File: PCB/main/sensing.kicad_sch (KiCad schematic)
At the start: 0 parts

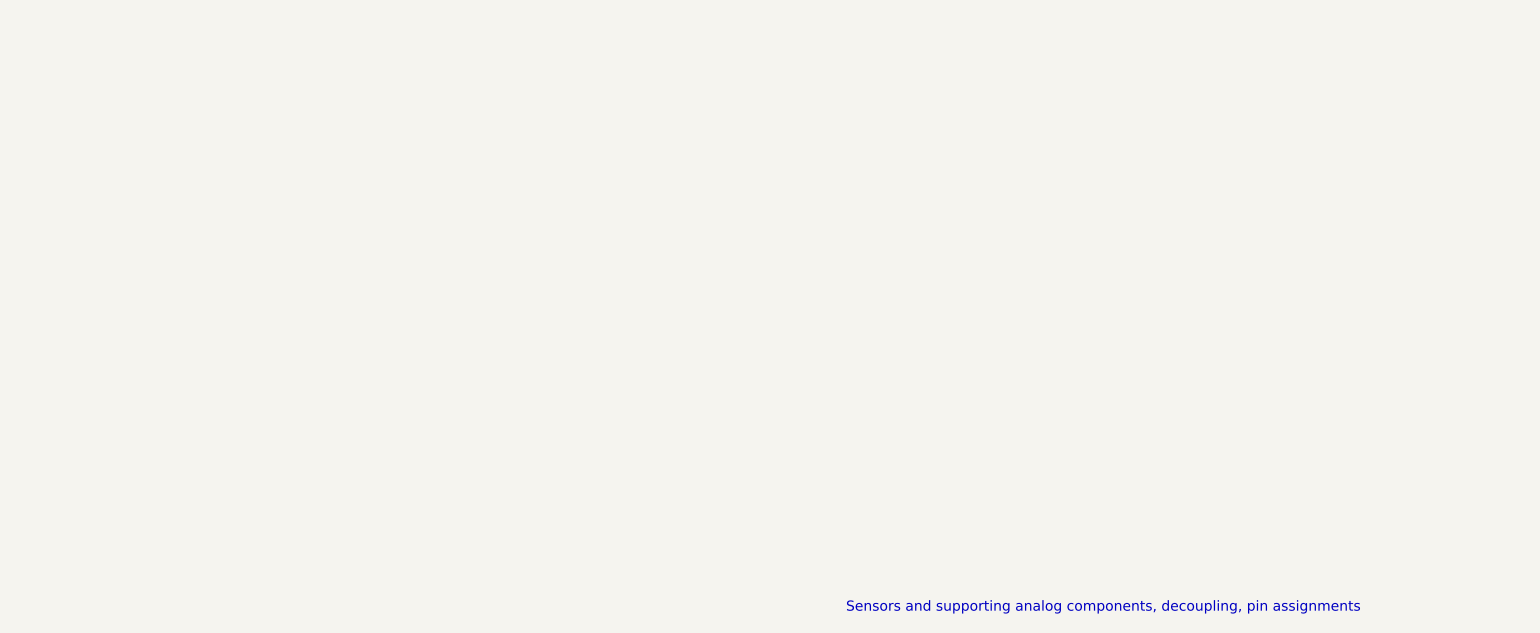
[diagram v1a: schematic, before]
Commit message: Added sensing schematic
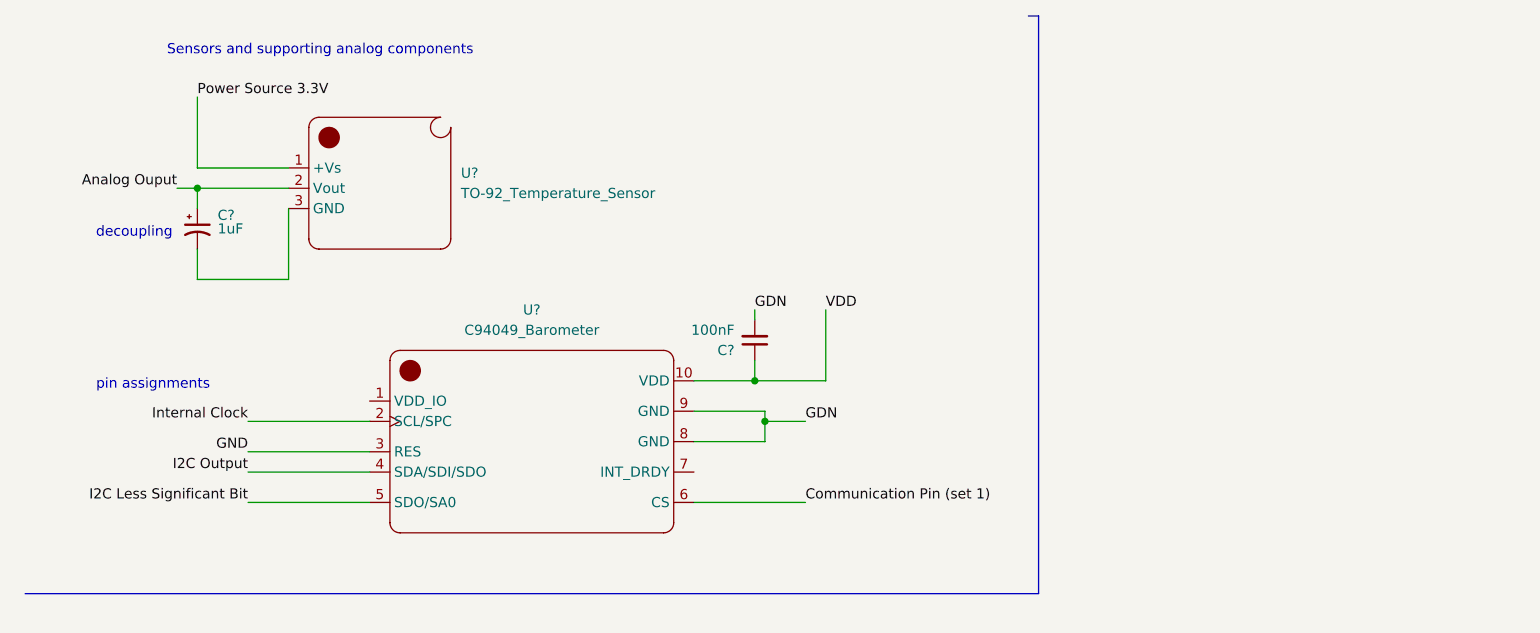
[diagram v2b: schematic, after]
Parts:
- added C?: 1uF, symbol Device:C_Polarized_Small_US
- added C?: 100nF, symbol Device:C_Small
- added U?: TO-92_Temperature_Sensor, symbol AAA 3088F:TO-92_Temperature_Sensor
- added U?: C94049_Barometer, symbol AAA 3088F:_C94049_Barometer
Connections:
- new net: C?.2, U?.3 (GND)
- new net Analog Ouput: C?.1, U?.2 (Vout)
- new net Communication Pin (set 1): U?.6 (CS)
- new net GDN: C?.2, U?.8 (GND), U?.9 (GND)
- new net GND: U?.3 (RES)
- new net I2C Less Significant Bit: U?.5 (SDO/SA0)
- new net I2C Output: U?.4 (SDA/SDI/SDO)
- new net Internal Clock: U?.2 (SCL/SPC)
- new net Power Source 3.3V: U?.1 (+Vs)
- new net VDD: C?.1, U?.10 (VDD)
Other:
- note added: "Sensors and supporting analog components"
- note added: "decoupling"
- note added: "pin assignments"
- note removed: "Sensors and supporting analog components, decoupling, pin assignments"
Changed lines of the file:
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@@
 (kicad_sch (version 20211123) (generator eeschema)
   (paper "A4")
-  (text "Sensors and supporting analog components, decoupling, pin assignments"
-    (at 115.57 86.36 0)
+  (junction (at 34.29 33.02) (diameter 0) (color 0 0 0 0)
+  )
+  (junction (at 105.41 62.23) (diameter 0) (color 0 0 0 0)
+  )
+  (junction (at 104.14 57.15) (diameter 0) (color 0 0 0 0)
+  )
+  (wire (pts (xy 104.14 57.15) (xy 104.14 54.61))
+    (stroke (width 0) (type default) (color 0 0 0 0))
+  )
+  (wire (pts (xy 96.52 57.15) (xy 104.14 57.15))
+    (stroke (width 0) (type default) (color 0 0 0 0))
+  )
+  (wire (pts (xy 31.75 33.02) (xy 34.29 33.02))
+    (stroke (width 0) (type default) (color 0 0 0 0))
+  )
+  (wire (pts (xy 40.64 68.58) (xy 55.88 68.58))
+    (stroke (width 0) (type default) (color 0 0 0 0))
+  )
+  (wire (pts (xy 105.41 64.77) (xy 105.41 62.23))
+    (stroke (width 0) (type default) (color 0 0 0 0))
+  )
+  (wire (pts (xy 40.64 62.23) (xy 55.88 62.23))
+    (stroke (width 0) (type default) (color 0 0 0 0))
+  )
+  (polyline (pts (xy 12.7 83.82) (xy 139.7 83.82))
+    (stroke (width 0) (type default) (color 0 0 0 0))
+  )
+  (wire (pts (xy 34.29 30.48) (xy 34.29 21.59))
+    (stroke (width 0) (type default) (color 0 0 0 0))
+  )
+  (wire (pts (xy 40.64 72.39) (xy 55.88 72.39))
+    (stroke (width 0) (type default) (color 0 0 0 0))
+  )
+  (wire (pts (xy 45.72 35.56) (xy 45.72 44.45))
+    (stroke (width 0) (type default) (color 0 0 0 0))
+  )
+  (wire (pts (xy 96.52 72.39) (xy 110.49 72.39))
+    (stroke (width 0) (type default) (color 0 0 0 0))
+  )
+  (wire (pts (xy 34.29 33.02) (xy 34.29 35.56))
+    (stroke (width 0) (type default) (color 0 0 0 0))
+  )
+  (wire (pts (xy 104.14 57.15) (xy 113.03 57.15))
+    (stroke (width 0) (type default) (color 0 0 0 0))
+  )
+  (wire (pts (xy 104.14 48.26) (xy 104.14 49.53))
+    (stroke (width 0) (type default) (color 0 0 0 0))
+  )
+  (wire (pts (xy 113.03 57.15) (xy 113.03 48.26))
+    (stroke (width 0) (type default) (color 0 0 0 0))
+  )
+  (polyline (pts (xy 139.7 83.82) (xy 139.7 11.43))
+    (stroke (width 0) (type default) (color 0 0 0 0))
+  )
+  (wire (pts (xy 96.52 60.96) (xy 105.41 60.96))
+    (stroke (width 0) (type default) (color 0 0 0 0))
+  )
+  (wire (pts (xy 105.41 62.23) (xy 110.49 62.23))
+    (stroke (width 0) (type default) (color 0 0 0 0))
+  )
+  (wire (pts (xy 105.41 60.96) (xy 105.41 62.23))
+    (stroke (width 0) (type default) (color 0 0 0 0))
+  )
+  (wire (pts (xy 45.72 30.48) (xy 34.29 30.48))
+    (stroke (width 0) (type default) (color 0 0 0 0))
+  )
+  (wire (pts (xy 40.64 66.04) (xy 55.88 66.04))
+    (stroke (width 0) (type default) (color 0 0 0 0))
+  )
+  (wire (pts (xy 45.72 44.45) (xy 34.29 44.45))
+    (stroke (width 0) (type default) (color 0 0 0 0))
+  )
+  (wire (pts (xy 34.29 40.64) (xy 34.29 44.45))
+    (stroke (width 0) (type default) (color 0 0 0 0))
+  )
+  (wire (pts (xy 96.52 64.77) (xy 105.41 64.77))
+    (stroke (width 0) (type default) (color 0 0 0 0))
+  )
+  (polyline (pts (xy 139.7 11.43) (xy 138.43 11.43))
+    (stroke (width 0) (type default) (color 0 0 0 0))
+  )
+  (wire (pts (xy 34.29 33.02) (xy 45.72 33.02))
+    (stroke (width 0) (type default) (color 0 0 0 0))
+  )
+  (text "Sensors and supporting analog components" (at 30.48 16.51 0)
     (effects (font (size 1.27 1.27)) (justify left bottom))
   )
+  (text "decoupling" (at 21.59 39.37 0)
+    (effects (font (size 1.27 1.27)) (justify left bottom))
+  )
+  (text "pin assignments" (at 21.59 58.42 0)
+    (effects (font (size 1.27 1.27)) (justify left bottom))
+  )
+  (label "Analog Ouput" (at 31.75 33.02 180)
+    (effects (font (size 1.27 1.27)) (justify right bottom))
+  )
+  (label "GND" (at 40.64 66.04 180)
+    (effects (font (size 1.27 1.27)) (justify right bottom))
+  )
+  (label "GDN" (at 104.14 48.26 0)
+    (effects (font (size 1.27 1.27)) (justify left bottom))
+  )
+  (label "Power Source 3.3V" (at 34.29 21.59 0)
+    (effects (font (size 1.27 1.27)) (justify left bottom))
+  )
+  (label "I2C Less Significant Bit" (at 40.64 72.39 180)
+    (effects (font (size 1.27 1.27)) (justify right bottom))
+  )
+  (label "GDN" (at 110.49 62.23 0)
+    (effects (font (size 1.27 1.27)) (justify left bottom))
+  )
+  (label "Communication Pin (set 1)" (at 110.49 72.39 0)
+    (effects (font (size 1.27 1.27)) (justify left bottom))
+  )
+  (label "VDD" (at 113.03 48.26 0)
+    (effects (font (size 1.27 1.27)) (justify left bottom))
+  )
+  (label "Internal Clock" (at 40.64 62.23 180)
+    (effects (font (size 1.27 1.27)) (justify right bottom))
+  )
+  (label "I2C Output" (at 40.64 68.58 180)
+    (effects (font (size 1.27 1.27)) (justify right bottom))
+  )
+  (symbol (lib_id "AAA 3088F:TO-92_Temperature_Sensor") (at 57.15 33.02 0) (unit 1)
+    (in_bom yes) (on_board yes) (fields_autoplaced)
+    (property "Reference" "U?" (id 0) (at 67.31 31.1149 0)
+      (effects (font (size 1.27 1.27)) (justify left))
+    )
+    (property "Value" "TO-92_Temperature_Sensor" (id 1) (at 67.31 33.6549 0)
+      (effects (font (size 1.27 1.27)) (justify left))
+    )
+    (property "Footprint" "" (id 2) (at 57.15 33.02 0)
+      (effects (font (size 1.27 1.27)) hide)
+    )
+    (property "Datasheet" "" (id 3) (at 57.15 33.02 0)
+      (effects (font (size 1.27 1.27)) hide)
+    )
+    (pin "1")
+    (pin "2")
+    (pin "3")
+  )
+  (symbol (lib_id "AAA 3088F:_C94049_Barometer") (at 76.2 67.31 0) (unit 1)
+    (in_bom yes) (on_board yes) (fields_autoplaced)
+    (property "Reference" "U?" (id 0) (at 76.2 48.26 0))
+    (property "Value" "C94049_Barometer" (id 1) (at 76.2 50.8 0))
+    (property "Footprint" "" (id 2) (at 76.2 67.31 0)
+      (effects (font (size 1.27 1.27)) hide)
+    )
+    (property "Datasheet" "" (id 3) (at 76.2 67.31 0)
+      (effects (font (size 1.27 1.27)) hide)
+    )
+    (pin "1")
+    (pin "10")
+    (pin "2")
+    (pin "3")
+    (pin "4")
+    (pin "5")
+    (pin "6")
+    (pin "7")
+    (pin "8")
+    (pin "9")
+  )
+  (symbol (lib_id "Device:C_Polarized_Small_US") (at 34.29 38.1 0) (unit 1)
+    (in_bom yes) (on_board yes)
+    (property "Reference" "C?" (id 0) (at 36.83 36.3981 0)
+      (effects (font (size 1.27 1.27)) (justify left))
+    )
+    (property "Value" "1uF" (id 1) (at 36.83 38.1 0)
+      (effects (font (size 1.27 1.27)) (justify left))
+    )
+    (property "Footprint" "" (id 2) (at 34.29 38.1 0)
+      (effects (font (size 1.27 1.27)) hide)
+    )
+    (property "Datasheet" "~" (id 3) (at 34.29 38.1 0)
+      (effects (font (size 1.27 1.27)) hide)
+    )
+    (pin "1")
+    (pin "2")
+  )
+  (symbol (lib_id "Device:C_Small") (at 104.14 52.07 180) (unit 1)
+    (in_bom yes) (on_board yes) (fields_autoplaced)
+    (property "Reference" "C?" (id 0) (at 101.6 53.3338 0)
+      (effects (font (size 1.27 1.27)) (justify left))
+    )
+    (property "Value" "100nF" (id 1) (at 101.6 50.7938 0)
+      (effects (font (size 1.27 1.27)) (justify left))
+    )
+    (property "Footprint" "" (id 2) (at 104.14 52.07 0)
+      (effects (font (size 1.27 1.27)) hide)
+    )
+    (property "Datasheet" "~" (id 3) (at 104.14 52.07 0)
+      (effects (font (size 1.27 1.27)) hide)
+    )
+    (pin "1")
+    (pin "2")
+  )
 )
